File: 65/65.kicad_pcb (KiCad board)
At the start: 2 copper layers, 318.3 x 104.1 mm, 152 parts, among them J2 USB_C_Receptacle_USB2.0_14P, K1 ESC, K10 9(, K11 0), K12 -_, K13 +=, K14 Backspace, K15 Delete, K16 Tab, K17 Q, K18 W, K19 E, K2 1!, K20 R, K21 T, K22 Y, K23 U, K24 I, K25 O, K26 P, K27 [{, K28 ]}, K29 \|, K3 2@, K30 Home, K31 Caps, K32 A, K33 S, K34 D, K35 F, K36 G, K37 H, K38 J, K39 K, K4 3#, K40 L, K41 ;:, K42 '", K43 Enter, K44 LShift, K45 Z, K46 X, K47 C, K48 V, K49 B, K5 4$, K50 N, K51 M, K52 ,<, K53 .>, K54 /?, K55 RShift, K56 Up, K57 LCtrl, K58 Windows, K59 LAlt, K6 5%, K60 Space, K61 RAlt, K62 Fn, K63 RCtrl, K64 Left, K65 Down, K66 Right, K7 6^, K8 7&, K9 8*, SW1 SW_Push, U1 USBLC6-2SC6, U2 ATmega32U4-A, Y2 Crystal_GND24

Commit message: No errors on design checker, will now be moving around the traces to make the board look a lil nicer
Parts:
- J2: footprint Connector_USB:USB_C_Receptacle_GCT_USB4105-xx-A_16P_TopMnt_Horizontal -> Connector_USB:USB_C_Receptacle_HRO_TYPE-C-31-M-12
- moved R2 24.6 mm to (356.8, 158.6)
- moved SW1 5.82 mm to (354.5, 164.5)
- moved R1 1.42 mm to (339.4, 151.5), turned to -90 degrees
- moved R6 1.34 mm to (200.2, 100.8)
- moved C2 0.56 mm to (335.8, 148.4)
- moved R5 0.20 mm to (205.3, 101.4)
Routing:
- net GND: track 34.2 -> 26.6 mm, vias 13 -> 15
- net /Row 1: track 319.5 -> 313.2 mm
- net +5V: track 290.8 -> 285.3 mm
- net /Col 8: track 247.6 -> 245.2 mm
- net /Reset: track 51.1 -> 53.4 mm, vias 4 -> 2
- net Net-(J2-CC1): track 6.25 -> 4.44 mm
- net /Row 2: track 275.5 -> 273.9 mm
- net /Col 14: track 104.9 -> 105.9 mm

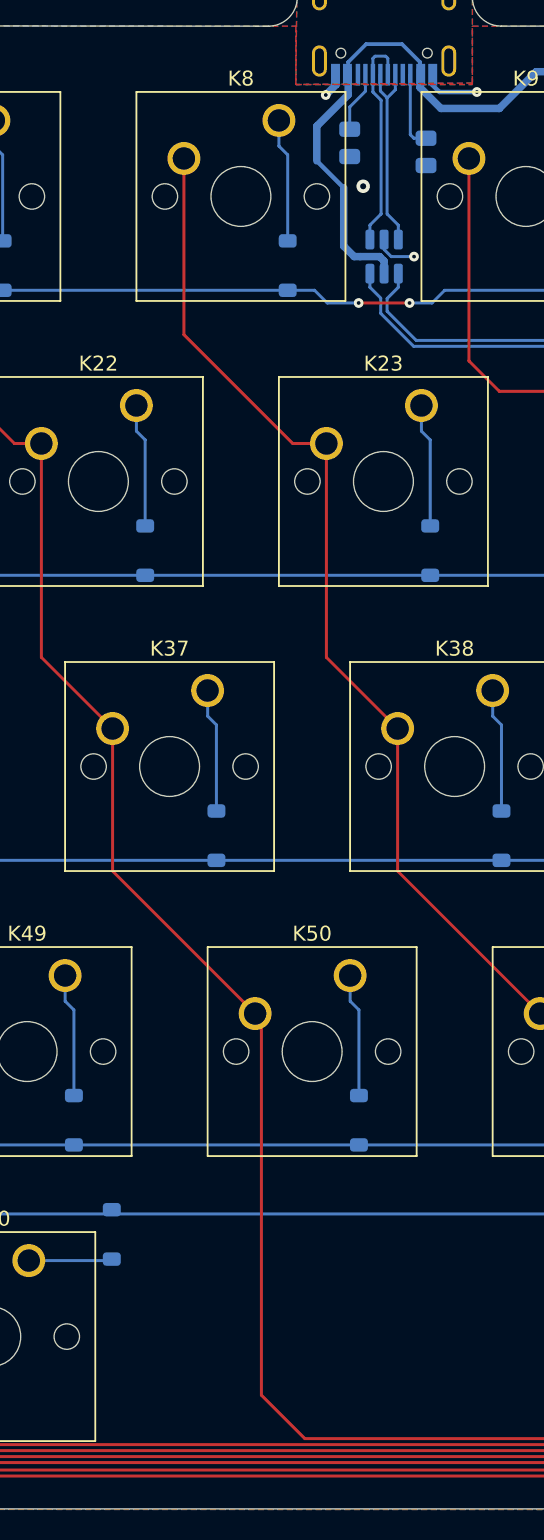
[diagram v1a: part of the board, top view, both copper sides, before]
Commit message: added keyboard config firmware
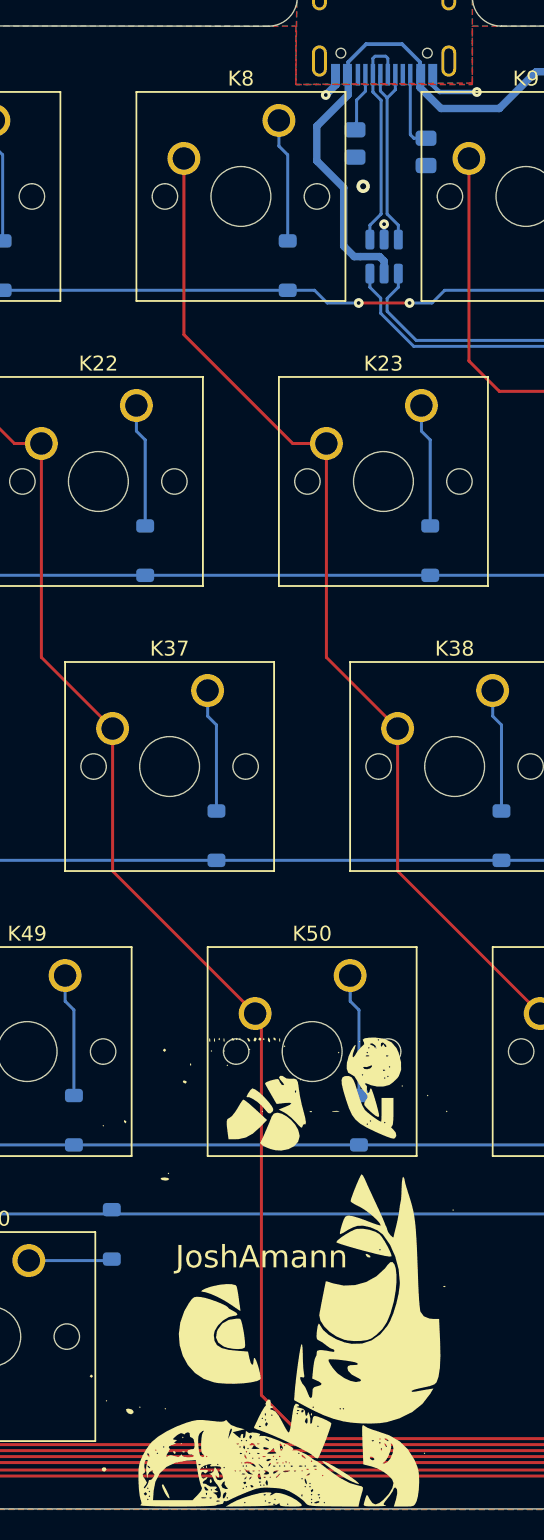
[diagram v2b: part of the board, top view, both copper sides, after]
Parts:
- added JoshAmann: LOGO, LOGO, F.Cu at (195.3, 176.2)
- moved R6 0.36 mm to (200.6, 100.8)
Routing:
- net GND: track 26.6 -> 24.8 mm
